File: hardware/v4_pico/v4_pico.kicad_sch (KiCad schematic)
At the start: 102 parts, among them J1 joystick, J10 ON/OFF, J11 MIDI IN bk: 5 R: 4, J2 LED strip, J3 SSD1306 SPI, J4 MIDI OUT Y:M5 - R:M4, J5 Batt, J6 Neck - Y:O BK:B R:3.3, J7 01x03, J8 MXP5010, J9 Thumb, Q1 2N7000, SW1 SW_DIP_x01, U1 74HC165, U2 74HC165, U3 74HC165, U4 Pico, U5 FJ08K, U6 6N138, U7 MCP3002

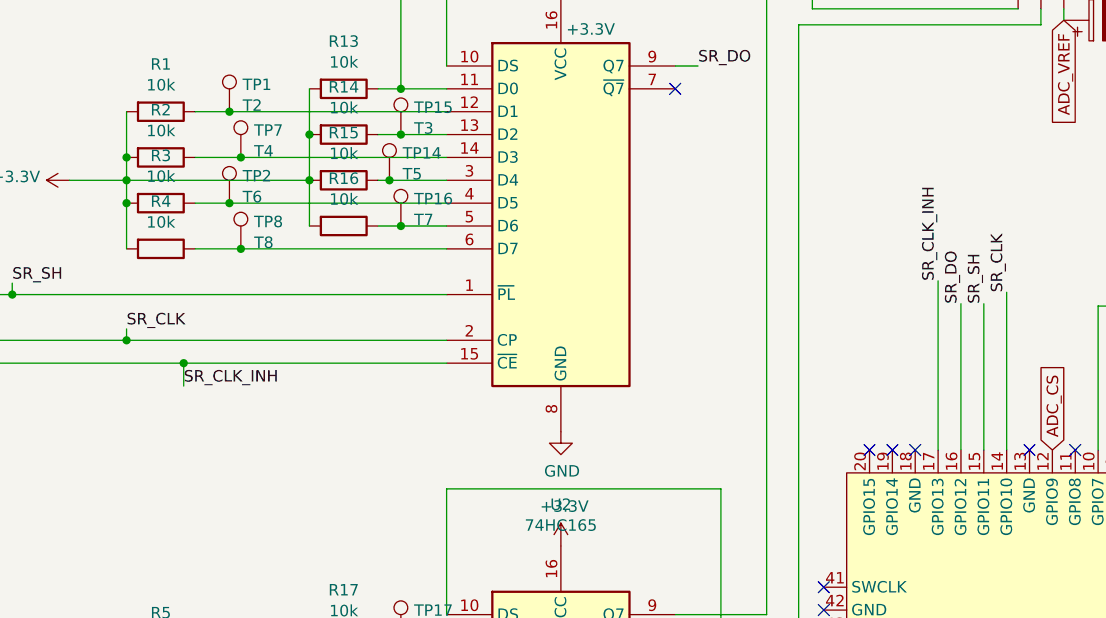
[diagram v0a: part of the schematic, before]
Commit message: Adapted and tested shift registers on SPI1
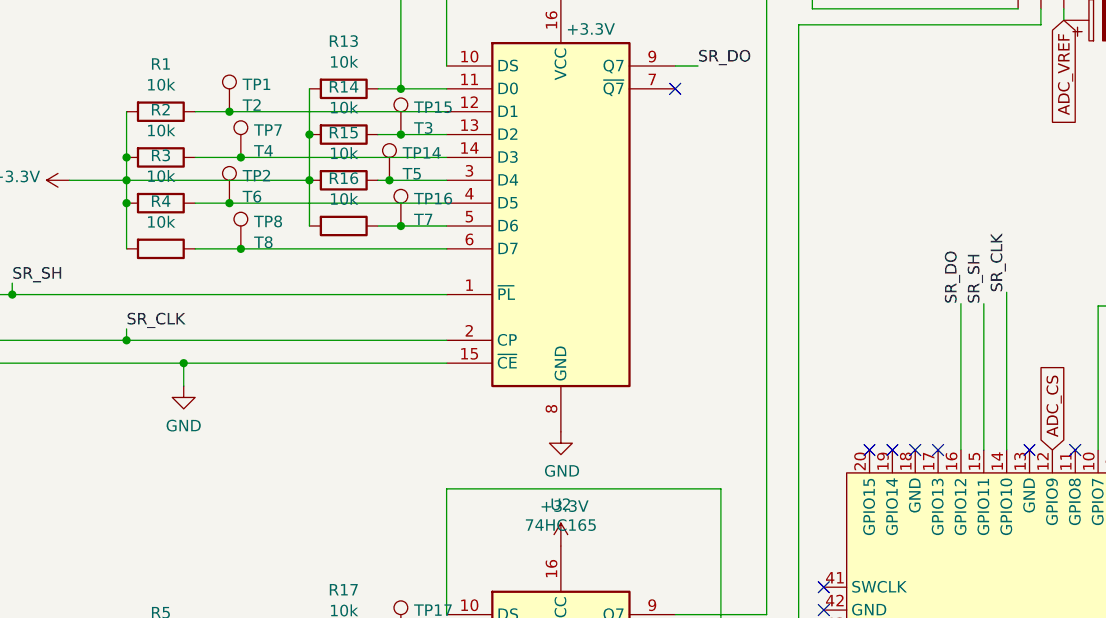
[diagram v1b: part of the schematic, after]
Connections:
- net GND: now also U1.15 (~{CE}), U2.15 (~{CE}), U3.15 (~{CE})
- removed net SR_CLK_INH: U1.15 (~{CE}), U2.15 (~{CE}), U3.15 (~{CE}), U4.17 (GPIO13)
- no-connect marks 25 -> 26
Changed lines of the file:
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@@
   (no_connect (at 119.38 73.152))
   (no_connect (at 124.46 73.152))
+  (no_connect (at 127 73.152))
   (no_connect (at 137.16 73.152))
   (no_connect (at 97.79 157.48))
@@
     (stroke (width 0) (type default) (color 0 0 0 0))
   )
-  (wire (pts (xy 127 54.356) (xy 127 73.152))
-    (stroke (width 0) (type default) (color 0 0 0 0))
-  )
   (wire (pts (xy 102.87 77.47) (xy 102.87 154.94))
     (stroke (width 0) (type default) (color 0 0 0 0))
@@
     (effects (font (size 1.27 1.27)) (justify left bottom))
   )
-  (label "SR_CLK_INH" (at 43.18 66.04 0)
-    (effects (font (size 1.27 1.27)) (justify left bottom))
-  )
   (label "SR_SH" (at 132.08 56.896 90)
     (effects (font (size 1.27 1.27)) (justify left bottom))
@@
     (effects (font (size 1.27 1.27)) (justify left bottom))
   )
-  (label "SR_CLK_INH" (at 127 54.356 90)
-    (effects (font (size 1.27 1.27)) (justify left bottom))
-  )
   (label "SR_SH" (at 24.13 54.61 0)
     (effects (font (size 1.27 1.27)) (justify left bottom))
@@
     (pin "1")
   )
+  (symbol (lib_id "power:GND") (at 43.18 66.04 0) (unit 1)
+    (in_bom yes) (on_board yes) (fields_autoplaced)
+    (property "Reference" "#PWR?" (id 0) (at 43.18 72.39 0)
+      (effects (font (size 1.27 1.27)) hide)
+    )
+    (property "Value" "GND" (id 1) (at 43.18 70.4834 0))
+    (property "Footprint" "" (id 2) (at 43.18 66.04 0)
+      (effects (font (size 1.27 1.27)) hide)
+    )
+    (property "Datasheet" "" (id 3) (at 43.18 66.04 0)
+      (effects (font (size 1.27 1.27)) hide)
+    )
+    (pin "1")
+  )
   (symbol (lib_id "power:GNDA") (at 150.876 110.49 0) (unit 1)
     (in_bom yes) (on_board yes) (fields_autoplaced)
@@
       (reference "#PWR0129") (unit 1) (value "GND") (footprint "")
     )
+    (path "/f60386b2-e051-4667-933b-1c1ceeda3b7c"
+      (reference "#PWR?") (unit 1) (value "GND") (footprint "")
+    )
     (path "/00000000-0000-0000-0000-000061cbc345"

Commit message: Started PCB
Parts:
- J11, J5: footprint Connector_JST:JST_XH_B2B-XH-A_1x02_P2.50mm_Vertical -> Connector_JST:JST_XH_S2B-XH-A_1x02_P2.50mm_Horizontal
- J2, J4, J6: footprint Connector_JST:JST_PH_B3B-PH-K_1x03_P2.00mm_Vertical -> Connector_JST:JST_PH_S3B-PH-K_1x03_P2.00mm_Horizontal
- U4: footprint RPi_Pico:RPi_Pico_SMD_TH -> Raspberry Pico:RPi_Pico_SMD_TH
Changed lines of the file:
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@@
       (effects (font (size 1.27 1.27)) (justify left))
     )
-    (property "Footprint" "Connector_JST:JST_XH_B2B-XH-A_1x02_P2.50mm_Vertical" (id 2) (at 279.654 40.132 0)
+    (property "Footprint" "Connector_JST:JST_XH_S2B-XH-A_1x02_P2.50mm_Horizontal" (id 2) (at 279.654 40.132 0)
       (effects (font (size 1.27 1.27)) hide)
     )
@@
       (effects (font (size 1.27 1.27)) (justify right))
     )
-    (property "Footprint" "Connector_JST:JST_PH_B3B-PH-K_1x03_P2.00mm_Vertical" (id 2) (at 199.39 38.1 0)
+    (property "Footprint" "Connector_JST:JST_PH_S3B-PH-K_1x03_P2.00mm_Horizontal" (id 2) (at 199.39 38.1 0)
       (effects (font (size 1.27 1.27)) hide)
     )
@@
       (effects (font (size 1.27 1.27)) (justify right))
     )
-    (property "Footprint" "Connector_JST:JST_PH_B3B-PH-K_1x03_P2.00mm_Vertical" (id 2) (at 181.102 157.48 0)
+    (property "Footprint" "Connector_JST:JST_PH_S3B-PH-K_1x03_P2.00mm_Horizontal" (id 2) (at 181.102 157.48 0)
       (effects (font (size 1.27 1.27)) hide)
     )
@@
       (effects (font (size 1.27 1.27)) (justify right))
     )
-    (property "Footprint" "Connector_JST:JST_PH_B3B-PH-K_1x03_P2.00mm_Vertical" (id 2) (at 138.43 19.05 0)
+    (property "Footprint" "Connector_JST:JST_PH_S3B-PH-K_1x03_P2.00mm_Horizontal" (id 2) (at 138.43 19.05 0)
       (effects (font (size 1.27 1.27)) hide)
     )
@@
       (effects (font (size 1.27 1.27)) (justify left))
     )
-    (property "Footprint" "Connector_JST:JST_XH_B2B-XH-A_1x02_P2.50mm_Vertical" (id 2) (at 226.822 70.104 0)
+    (property "Footprint" "Connector_JST:JST_XH_S2B-XH-A_1x02_P2.50mm_Horizontal" (id 2) (at 226.822 70.104 0)
       (effects (font (size 1.27 1.27)) hide)
     )
@@
       (effects (font (size 1.27 1.27)) (justify left))
     )
-    (property "Footprint" "RPi_Pico:RPi_Pico_SMD_TH" (id 2) (at 143.51 90.932 90)
+    (property "Footprint" "Raspberry Pico:RPi_Pico_SMD_TH" (id 2) (at 143.51 90.932 90)
       (effects (font (size 1.27 1.27)) hide)
     )
@@
   (symbol (lib_id "power:GND") (at 43.18 66.04 0) (unit 1)
     (in_bom yes) (on_board yes) (fields_autoplaced)
-    (property "Reference" "#PWR?" (id 0) (at 43.18 72.39 0)
+    (property "Reference" "#PWR07" (id 0) (at 43.18 72.39 0)
       (effects (font (size 1.27 1.27)) hide)
     )
@@
       (reference "#PWR06") (unit 1) (value "GND") (footprint "")
     )
+    (path "/f60386b2-e051-4667-933b-1c1ceeda3b7c"
+      (reference "#PWR07") (unit 1) (value "GND") (footprint "")
+    )
     (path "/c74a8e6d-ad6b-4b8f-b981-28df0ace3a1f"
       (reference "#PWR08") (unit 1) (value "GNDA") (footprint "")
@@
       (reference "#PWR0129") (unit 1) (value "GND") (footprint "")
     )
-    (path "/f60386b2-e051-4667-933b-1c1ceeda3b7c"
-      (reference "#PWR?") (unit 1) (value "GND") (footprint "")
-    )
     (path "/00000000-0000-0000-0000-000061cbc345"
       (reference "C1") (unit 1) (value "1000u Ch") (footprint "Capacitor_THT:CP_Radial_D8.0mm_P3.50mm")
@@
     )
     (path "/00000000-0000-0000-0000-000061c7df83"
-      (reference "J2") (unit 1) (value "LED strip") (footprint "Connector_JST:JST_PH_B3B-PH-K_1x03_P2.00mm_Vertical")
+      (reference "J2") (unit 1) (value "LED strip") (footprint "Connector_JST:JST_PH_S3B-PH-K_1x03_P2.00mm_Horizontal")
     )
     (path "/00000000-0000-0000-0000-000061afd10c"
@@
     )
     (path "/00000000-0000-0000-0000-000061c4a21d"
-      (reference "J4") (unit 1) (value "MIDI OUT Y:M5 - R:M4") (footprint "Connector_JST:JST_PH_B3B-PH-K_1x03_P2.00mm_Vertical")
+      (reference "J4") (unit 1) (value "MIDI OUT Y:M5 - R:M4") (footprint "Connector_JST:JST_PH_S3B-PH-K_1x03_P2.00mm_Horizontal")
     )
     (path "/00000000-0000-0000-0000-000061bf481a"
-      (reference "J5") (unit 1) (value "Batt") (footprint "Connector_JST:JST_XH_B2B-XH-A_1x02_P2.50mm_Vertical")
+      (reference "J5") (unit 1) (value "Batt") (footprint "Connector_JST:JST_XH_S2B-XH-A_1x02_P2.50mm_Horizontal")
     )
     (path "/00000000-0000-0000-0000-000061e7f82b"
-      (reference "J6") (unit 1) (value "Neck - Y:O BK:B R:3.3") (footprint "Connector_JST:JST_PH_B3B-PH-K_1x03_P2.00mm_Vertical")
+      (reference "J6") (unit 1) (value "Neck - Y:O BK:B R:3.3") (footprint "Connector_JST:JST_PH_S3B-PH-K_1x03_P2.00mm_Horizontal")
     )
     (path "/00000000-0000-0000-0000-000061edf687"
@@
     )
     (path "/521fec83-782b-47eb-b1d7-f5cb6fa7f991"
-      (reference "J11") (unit 1) (value "MIDI IN bk: 5 R: 4") (footprint "Connector_JST:JST_XH_B2B-XH-A_1x02_P2.50mm_Vertical")
+      (reference "J11") (unit 1) (value "MIDI IN bk: 5 R: 4") (footprint "Connector_JST:JST_XH_S2B-XH-A_1x02_P2.50mm_Horizontal")
     )
     (path "/d6a7f71a-4da6-4997-9a3d-af77c0308253"
@@
     )
     (path "/548a6b39-284d-44c8-9c5c-d9af1c8c3533"
-      (reference "U4") (unit 1) (value "Pico") (footprint "RPi_Pico:RPi_Pico_SMD_TH")
+      (reference "U4") (unit 1) (value "Pico") (footprint "Raspberry Pico:RPi_Pico_SMD_TH")
     )
     (path "/497d404a-5f3e-42dc-8f03-00c98c45a389"

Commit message: Work on PCB
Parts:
- C7: footprint Capacitor_THT:CP_Radial_D7.5mm_P2.50mm -> Capacitor_THT:CP_Radial_D6.3mm_P2.50mm
- J3: footprint Connector_PinSocket_2.54mm:PinSocket_1x07_P2.54mm_Vertical -> Connector_JST:JST_PH_S7B-PH-K_1x07_P2.00mm_Horizontal
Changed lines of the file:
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@@
     (property "Reference" "J3" (id 0) (at 157.988 30.099 90))
     (property "Value" "SSD1306 SPI" (id 1) (at 157.988 32.4104 90))
-    (property "Footprint" "Connector_PinSocket_2.54mm:PinSocket_1x07_P2.54mm_Vertical" (id 2) (at 157.48 34.29 0)
+    (property "Footprint" "Connector_JST:JST_PH_S7B-PH-K_1x07_P2.00mm_Horizontal" (id 2) (at 157.48 34.29 0)
       (effects (font (size 1.27 1.27)) hide)
     )
@@
       (effects (font (size 1.27 1.27)) (justify right))
     )
-    (property "Footprint" "Capacitor_THT:CP_Radial_D7.5mm_P2.50mm" (id 2) (at 173.5328 68.326 0)
+    (property "Footprint" "Capacitor_THT:CP_Radial_D6.3mm_P2.50mm" (id 2) (at 173.5328 68.326 0)
       (effects (font (size 1.27 1.27)) hide)
     )
@@
     )
     (path "/7645b832-44a0-4178-932a-e01c230c6392"
-      (reference "C7") (unit 1) (value "100u") (footprint "Capacitor_THT:CP_Radial_D7.5mm_P2.50mm")
+      (reference "C7") (unit 1) (value "100u") (footprint "Capacitor_THT:CP_Radial_D6.3mm_P2.50mm")
     )
     (path "/6ea2bc83-6e60-44b0-9fd6-b93a1503a50c"
@@
     )
     (path "/00000000-0000-0000-0000-000061afd10c"
-      (reference "J3") (unit 1) (value "SSD1306 SPI") (footprint "Connector_PinSocket_2.54mm:PinSocket_1x07_P2.54mm_Vertical")
+      (reference "J3") (unit 1) (value "SSD1306 SPI") (footprint "Connector_JST:JST_PH_S7B-PH-K_1x07_P2.00mm_Horizontal")
     )
     (path "/00000000-0000-0000-0000-000061c4a21d"

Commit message: Trying to place everythin on pcb...
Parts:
- J10: footprint Connector_JST:JST_XH_B2B-XH-A_1x02_P2.50mm_Vertical -> Connector_JST:JST_XH_S2B-XH-A_1x02_P2.50mm_Horizontal
- J3: footprint Connector_JST:JST_PH_S7B-PH-K_1x07_P2.00mm_Horizontal -> Connector_JST:JST_PH_B7B-PH-K_1x07_P2.00mm_Vertical
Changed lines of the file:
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@@
     (property "Reference" "J3" (id 0) (at 157.988 30.099 90))
     (property "Value" "SSD1306 SPI" (id 1) (at 157.988 32.4104 90))
-    (property "Footprint" "Connector_JST:JST_PH_S7B-PH-K_1x07_P2.00mm_Horizontal" (id 2) (at 157.48 34.29 0)
+    (property "Footprint" "Connector_JST:JST_PH_B7B-PH-K_1x07_P2.00mm_Vertical" (id 2) (at 157.48 34.29 0)
       (effects (font (size 1.27 1.27)) hide)
     )
@@
     (property "Reference" "J10" (id 0) (at 264.033 33.435 0))
     (property "Value" "ON/OFF" (id 1) (at 264.033 35.9719 0))
-    (property "Footprint" "Connector_JST:JST_XH_B2B-XH-A_1x02_P2.50mm_Vertical" (id 2) (at 263.398 40.132 0)
+    (property "Footprint" "Connector_JST:JST_XH_S2B-XH-A_1x02_P2.50mm_Horizontal" (id 2) (at 263.398 40.132 0)
       (effects (font (size 1.27 1.27)) hide)
     )
@@
     )
     (path "/00000000-0000-0000-0000-000061afd10c"
-      (reference "J3") (unit 1) (value "SSD1306 SPI") (footprint "Connector_JST:JST_PH_S7B-PH-K_1x07_P2.00mm_Horizontal")
+      (reference "J3") (unit 1) (value "SSD1306 SPI") (footprint "Connector_JST:JST_PH_B7B-PH-K_1x07_P2.00mm_Vertical")
     )
     (path "/00000000-0000-0000-0000-000061c4a21d"
@@
     )
     (path "/51855148-c4cd-4659-9355-2a7b71541229"
-      (reference "J10") (unit 1) (value "ON/OFF") (footprint "Connector_JST:JST_XH_B2B-XH-A_1x02_P2.50mm_Vertical")
+      (reference "J10") (unit 1) (value "ON/OFF") (footprint "Connector_JST:JST_XH_S2B-XH-A_1x02_P2.50mm_Horizontal")
     )
     (path "/521fec83-782b-47eb-b1d7-f5cb6fa7f991"

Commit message: Initial routing
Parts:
- removed TP13: 3.3, TestPoint:TestPoint_THTPad_2.5x2.5mm_Drill1.2mm, symbol Connector:TestPoint
- Q1: footprint Package_TO_SOT_THT:TO-92_Inline -> Package_TO_SOT_THT:TO-92L_HandSolder
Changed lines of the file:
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@@
     (stroke (width 0) (type default) (color 0 0 0 0))
   )
-  (wire (pts (xy 177.8 21.59) (xy 184.15 21.59))
-    (stroke (width 0) (type default) (color 0 0 0 0))
-  )
   (wire (pts (xy 113.03 15.24) (xy 67.31 15.24))
     (stroke (width 0) (type default) (color 0 0 0 0))
@@
     (pin "3")
   )
-  (symbol (lib_id "Connector:TestPoint") (at 177.8 21.59 0) (unit 1)
-    (in_bom yes) (on_board yes)
-    (property "Reference" "TP13" (id 0) (at 179.2732 18.5928 0)
-      (effects (font (size 1.27 1.27)) (justify left))
-    )
-    (property "Value" "3.3" (id 1) (at 179.2732 20.9042 0)
-      (effects (font (size 1.27 1.27)) (justify left))
-    )
-    (property "Footprint" "TestPoint:TestPoint_THTPad_2.5x2.5mm_Drill1.2mm" (id 2) (at 182.88 21.59 0)
-      (effects (font (size 1.27 1.27)) hide)
-    )
-    (property "Datasheet" "~" (id 3) (at 182.88 21.59 0)
-      (effects (font (size 1.27 1.27)) hide)
-    )
-    (pin "1")
-  )
   (symbol (lib_id "Connector:TestPoint") (at 184.15 21.59 0) (unit 1)
     (in_bom yes) (on_board yes)
@@
       (effects (font (size 1.27 1.27)) (justify left))
     )
-    (property "Footprint" "Package_TO_SOT_THT:TO-92_Inline" (id 2) (at 165.1 131.953 0)
+    (property "Footprint" "Package_TO_SOT_THT:TO-92L_HandSolder" (id 2) (at 165.1 131.953 0)
       (effects (font (size 1.27 1.27) italic) (justify left) hide)
     )
@@
     )
     (path "/d6a7f71a-4da6-4997-9a3d-af77c0308253"
-      (reference "Q1") (unit 1) (value "2N7000") (footprint "Package_TO_SOT_THT:TO-92_Inline")
+      (reference "Q1") (unit 1) (value "2N7000") (footprint "Package_TO_SOT_THT:TO-92L_HandSolder")
     )
     (path "/00000000-0000-0000-0000-000061b28de3"
@@
       (reference "TP12") (unit 1) (value "T24") (footprint "TestPoint:TestPoint_THTPad_2.5x2.5mm_Drill1.2mm")
     )
-    (path "/00000000-0000-0000-0000-000061e93fa3"
-      (reference "TP13") (unit 1) (value "3.3") (footprint "TestPoint:TestPoint_THTPad_2.5x2.5mm_Drill1.2mm")
-    )
     (path "/00000000-0000-0000-0000-000061b86a37"

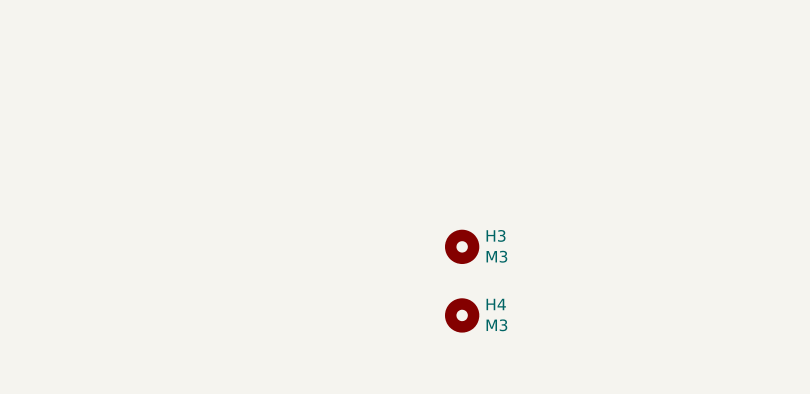
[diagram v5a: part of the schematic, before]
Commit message: Improved silk
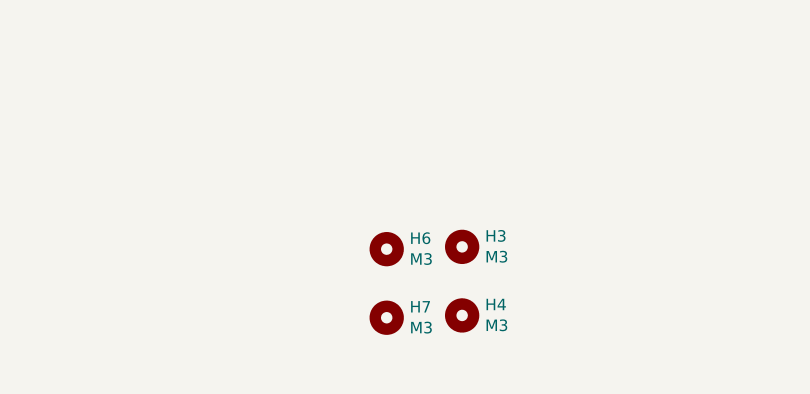
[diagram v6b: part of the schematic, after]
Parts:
- added H6, H7: M3, MountingHole:MountingHole_3.2mm_M3, symbol Mechanical:MountingHole
- U4: footprint Raspberry Pico:RPi_Pico_SMD_TH -> Raspberry Pico:RPi_Pico_TH
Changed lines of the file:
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@@
     (pin "1")
+  )
+  (symbol (lib_id "Mechanical:MountingHole") (at 163.068 187.198 0) (unit 1)
+    (in_bom yes) (on_board yes)
+    (property "Reference" "H6" (id 0) (at 165.608 186.0296 0)
+      (effects (font (size 1.27 1.27)) (justify left))
+    )
+    (property "Value" "M3" (id 1) (at 165.608 188.341 0)
+      (effects (font (size 1.27 1.27)) (justify left))
+    )
+    (property "Footprint" "MountingHole:MountingHole_3.2mm_M3" (id 2) (at 163.068 187.198 0)
+      (effects (font (size 1.27 1.27)) hide)
+    )
+    (property "Datasheet" "~" (id 3) (at 163.068 187.198 0)
+      (effects (font (size 1.27 1.27)) hide)
+    )
   )
   (symbol (lib_id "Switch:SW_DIP_x01") (at 221.234 139.954 90) (unit 1)
@@
       (effects (font (size 1.27 1.27)) (justify left))
     )
-    (property "Footprint" "Raspberry Pico:RPi_Pico_SMD_TH" (id 2) (at 143.51 90.932 90)
+    (property "Footprint" "Raspberry Pico:RPi_Pico_TH" (id 2) (at 143.51 90.932 90)
       (effects (font (size 1.27 1.27)) hide)
     )
@@
     (pin "1")
   )
+  (symbol (lib_id "Mechanical:MountingHole") (at 163.068 194.818 0) (unit 1)
+    (in_bom yes) (on_board yes)
+    (property "Reference" "H7" (id 0) (at 165.608 193.6496 0)
+      (effects (font (size 1.27 1.27)) (justify left))
+    )
+    (property "Value" "M3" (id 1) (at 165.608 195.961 0)
+      (effects (font (size 1.27 1.27)) (justify left))
+    )
+    (property "Footprint" "MountingHole:MountingHole_3.2mm_M3" (id 2) (at 163.068 194.818 0)
+      (effects (font (size 1.27 1.27)) hide)
+    )
+    (property "Datasheet" "~" (id 3) (at 163.068 194.818 0)
+      (effects (font (size 1.27 1.27)) hide)
+    )
+  )
   (symbol (lib_id "power:GNDA") (at 232.918 88.138 180) (unit 1)
     (in_bom yes) (on_board yes) (fields_autoplaced)
@@
       (reference "H5") (unit 1) (value "M3") (footprint "MountingHole:MountingHole_3.2mm_M3")
     )
+    (path "/2d002a73-5516-4c7c-a5de-f495a513c854"
+      (reference "H6") (unit 1) (value "M3") (footprint "MountingHole:MountingHole_3.2mm_M3")
+    )
+    (path "/c3c77499-0c99-48fd-98c8-a98114e8d5ad"
+      (reference "H7") (unit 1) (value "M3") (footprint "MountingHole:MountingHole_3.2mm_M3")
+    )
     (path "/00000000-0000-0000-0000-000061c0fcb8"
       (reference "J1") (unit 1) (value "joystick") (footprint "Connector_JST:JST_PH_B5B-PH-K_1x05_P2.00mm_Vertical")
@@
     )
     (path "/548a6b39-284d-44c8-9c5c-d9af1c8c3533"
-      (reference "U4") (unit 1) (value "Pico") (footprint "Raspberry Pico:RPi_Pico_SMD_TH")
+      (reference "U4") (unit 1) (value "Pico") (footprint "Raspberry Pico:RPi_Pico_TH")
     )
     (path "/497d404a-5f3e-42dc-8f03-00c98c45a389"
